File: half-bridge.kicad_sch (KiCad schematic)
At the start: 13 parts, among them Q7 IRLHS6242, Q8 IRLHS6242, U9 DGD05473FNQ-7

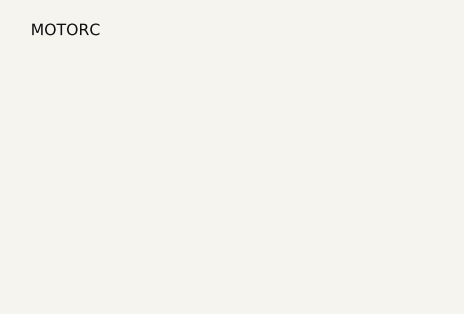
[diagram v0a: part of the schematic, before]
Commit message: finish schematic + footprints
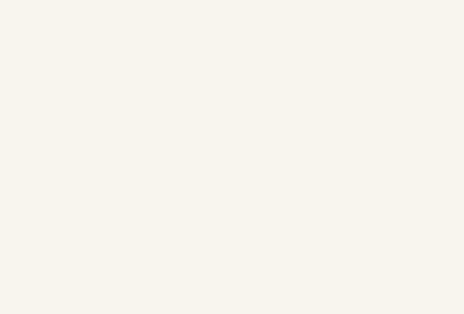
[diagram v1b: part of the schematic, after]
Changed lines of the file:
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@@
-		)
-	)
-	(label "MOTORC"
-		(at 8.0012 2.0957 180)
-		(effects
-			(font
-				(size 1.27 1.27)
-			)
-			(justify right bottom)
 		)
 	)
